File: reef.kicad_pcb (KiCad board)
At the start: 2 copper layers, 85 parts, among them J1 Conn_01x05_Female, J2 Conn_01x02_Male, U1 nice_nano, U2 TRRS, U3 TRRS

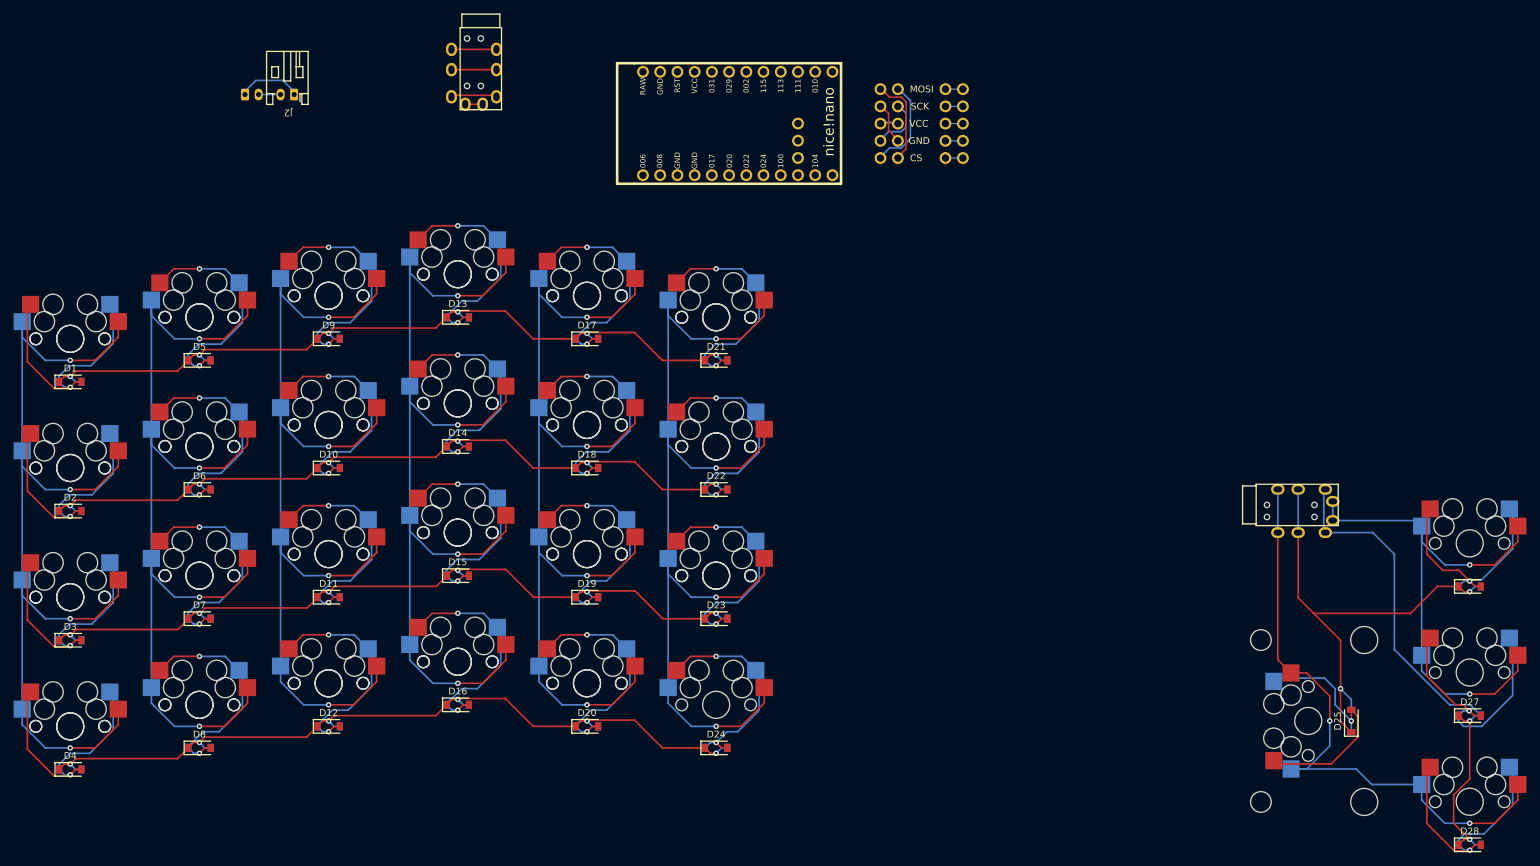
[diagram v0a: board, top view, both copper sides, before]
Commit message: Reversible via Jumper Pads
using solder jumper pads to make component footprints reversible
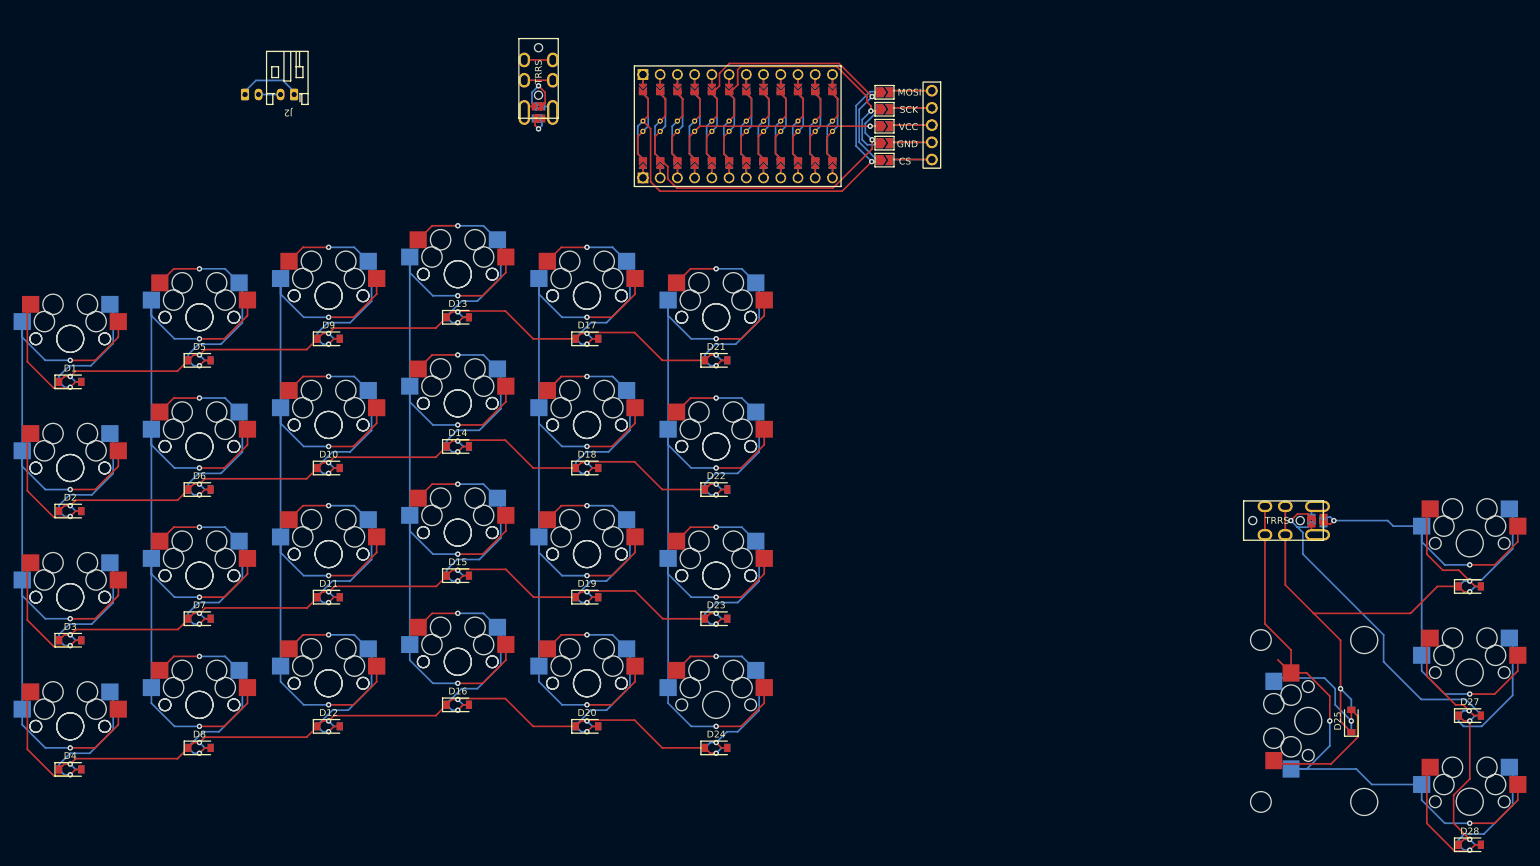
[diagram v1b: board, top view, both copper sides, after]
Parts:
- Display1: moved to F.Cu
- U1: footprint nice-nano-kicad:nice_nano -> keyboard_reversible:ProMicro
- U2, U3: footprint Keebio-Parts:TRRS-PJ-320A -> keyboard_reversible:PJ-320A
- moved U2 8.61 mm to (115.9, 24.6)
- moved Display1 4.57 mm to (188.3, 37.4), turned to -90 degrees
- moved U3 3.16 mm to (219.7, 95.9)
- moved J1 0.91 mm to (166.8, 37.8)
- moved U1 0.40 mm to (145.3, 37.7)
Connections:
- U1 pad 5: sck -> mosi
- U1 pad 6: mosi -> sck
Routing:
- net (no net): track 12.8 -> 63.3 mm
- net cs: track 13.2 -> 59.2 mm, vias 0 -> 1
- net gnd: track 9.38 -> 48.2 mm, vias 0 -> 1
- net sck: track 8.24 -> 36.6 mm, vias 0 -> 1
- net mosi: track 13.8 -> 41.5 mm, vias 0 -> 1
- net vcc: track 2.57 -> 29.0 mm, vias 0 -> 1
- net row_0: track 123.8 -> 121.4 mm
- net col_6: track 6.63 -> 4.20 mm
- net thr_0: track 69.8 -> 68.1 mm
- net thc_7: track 78.5 -> 80.2 mm, vias 2 -> 3
- net thr_1: track 76.3 -> 77.5 mm, vias 2 -> 3
- net thc_6: track 91.3 -> 92.3 mm
- net col_7: track 2.57 -> 3.48 mm, vias 0 -> 1
- net row_1: track 124.0 -> 124.5 mm, vias 6 -> 7

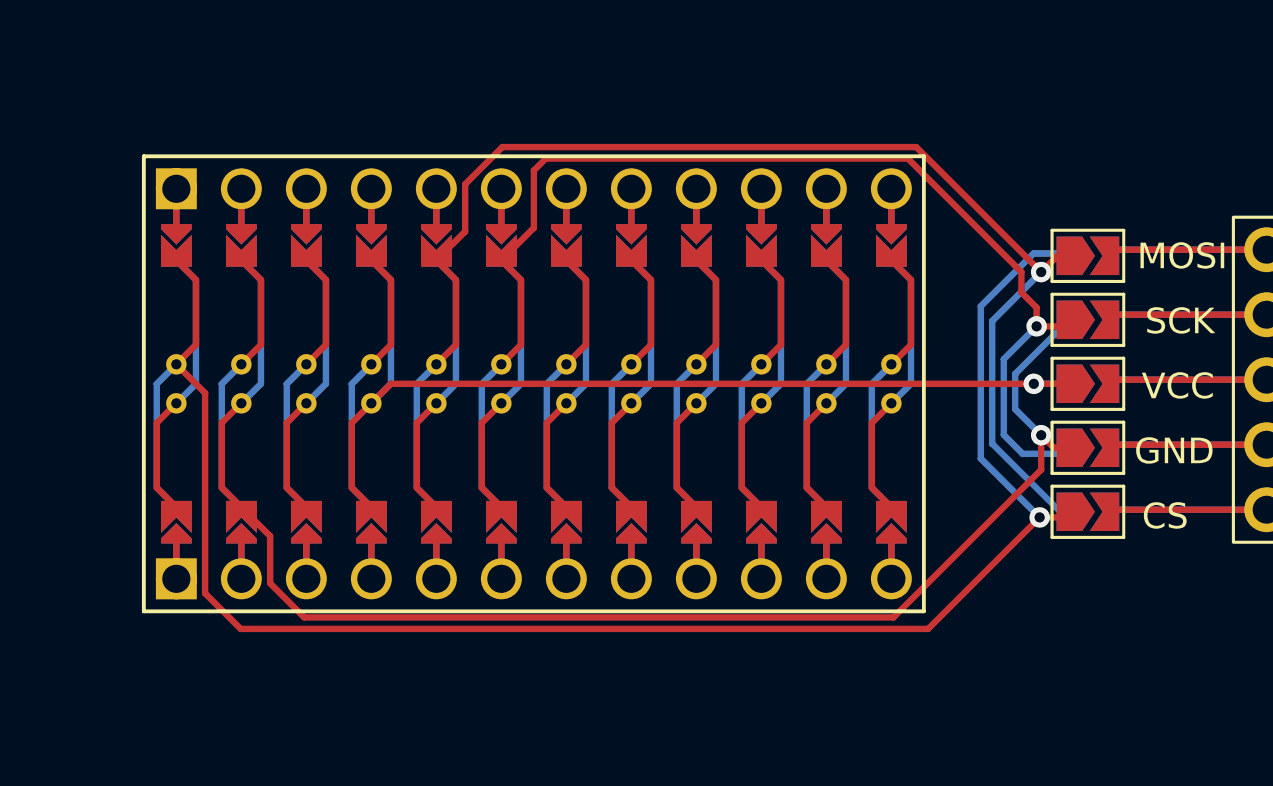
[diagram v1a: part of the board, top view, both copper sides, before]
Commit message: Display Routing
Traces for display should no longer interfere with routing columns and rows to their respective pins in an aesthetically pleasing manner...hopefully
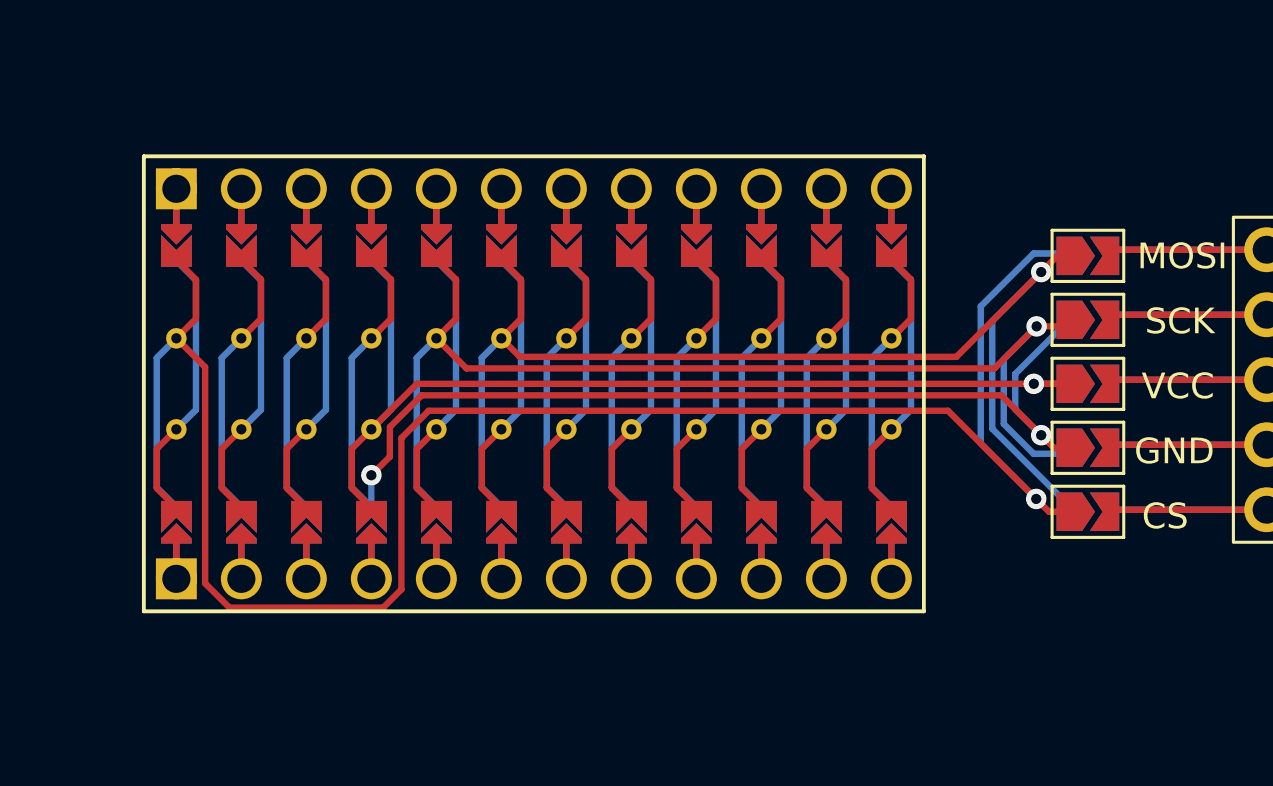
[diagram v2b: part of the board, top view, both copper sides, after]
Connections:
- U1 pad 5: mosi -> sck
- U1 pad 6: sck -> mosi
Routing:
- net gnd: track 48.2 -> 40.4 mm, vias 1 -> 2
- net cs: track 59.2 -> 65.3 mm
- net mosi: track 41.5 -> 35.5 mm
- net sck: track 36.6 -> 33.5 mm

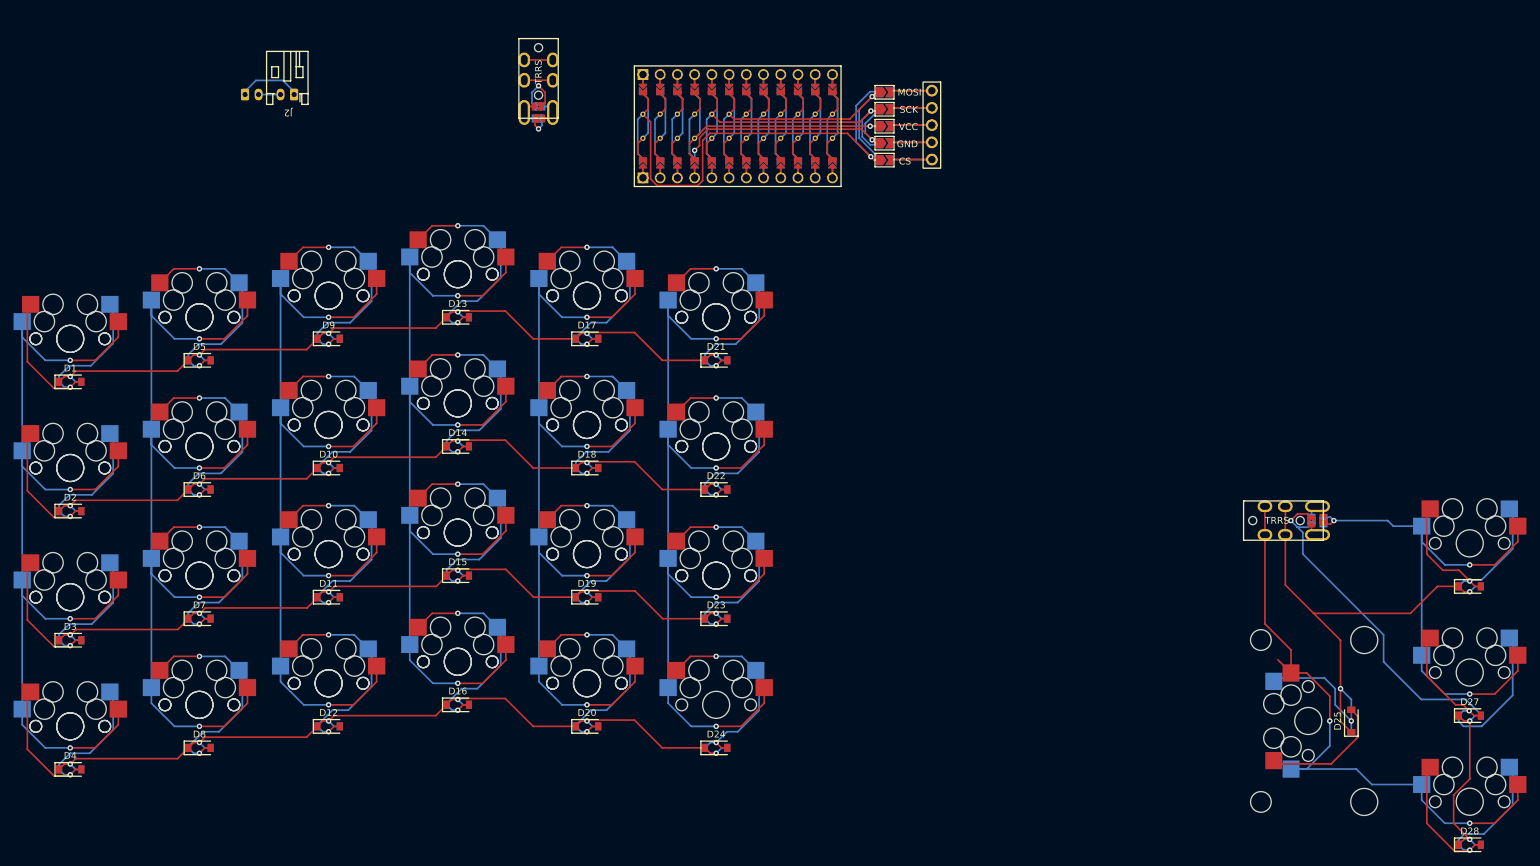
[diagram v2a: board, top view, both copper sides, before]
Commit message: Matrix Reroute
rerouted some matrix traces to connect to vias instead of going through diode pads
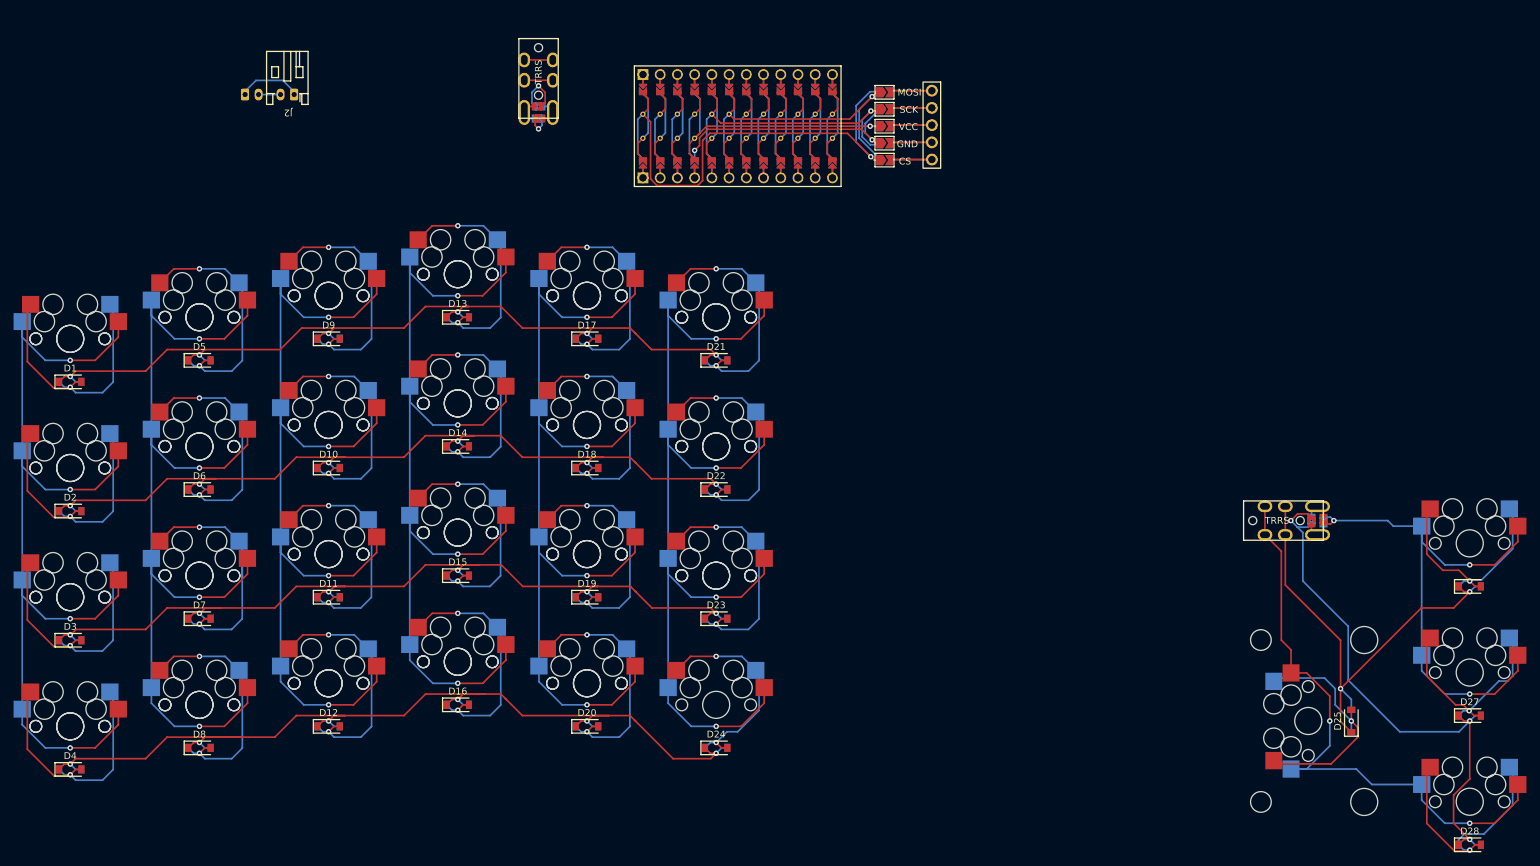
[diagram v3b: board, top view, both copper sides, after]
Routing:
- net row_3: track 117.2 -> 145.1 mm
- net row_2: track 117.2 -> 138.3 mm
- net row_1: track 124.5 -> 144.5 mm
- net row_0: track 121.4 -> 135.9 mm
- net Net-(D7-Pad2): track 34.0 -> 41.4 mm
- net Net-(D27-Pad2): track 37.7 -> 32.4 mm
- net thr_1: track 77.5 -> 82.0 mm
- net Net-(D17-Pad2): track 33.6 -> 36.5 mm
- net Net-(D13-Pad2): track 33.6 -> 36.5 mm
- net thc_6: track 92.3 -> 89.6 mm
- net Net-(D19-Pad2): track 33.6 -> 36.3 mm
- net Net-(D20-Pad2): track 33.6 -> 36.3 mm
- net Net-(D12-Pad2): track 33.6 -> 36.3 mm
- net Net-(D8-Pad2): track 33.6 -> 36.3 mm
- net Net-(D16-Pad2): track 33.6 -> 36.3 mm
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
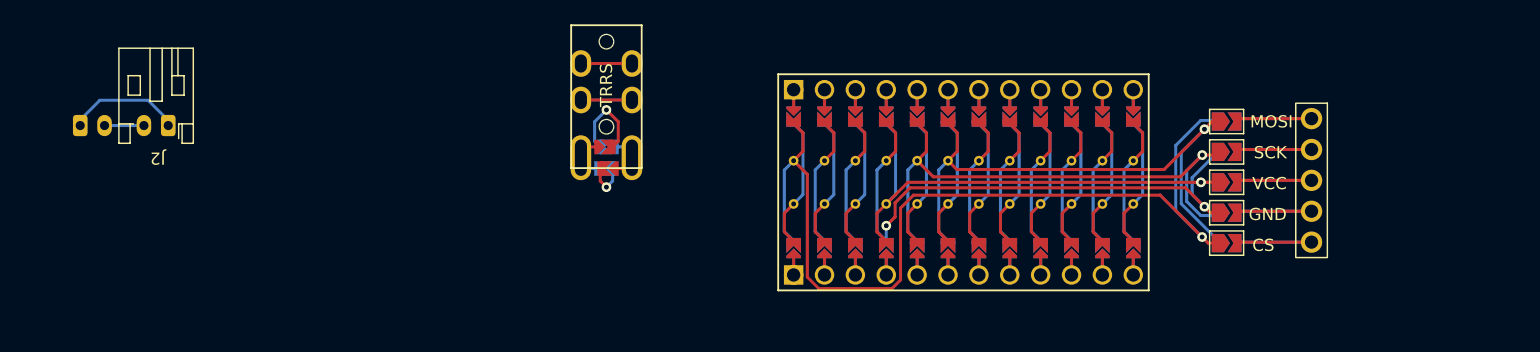
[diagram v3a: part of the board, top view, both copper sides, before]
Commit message: Routed Battery Connector
routed traces for battery connector
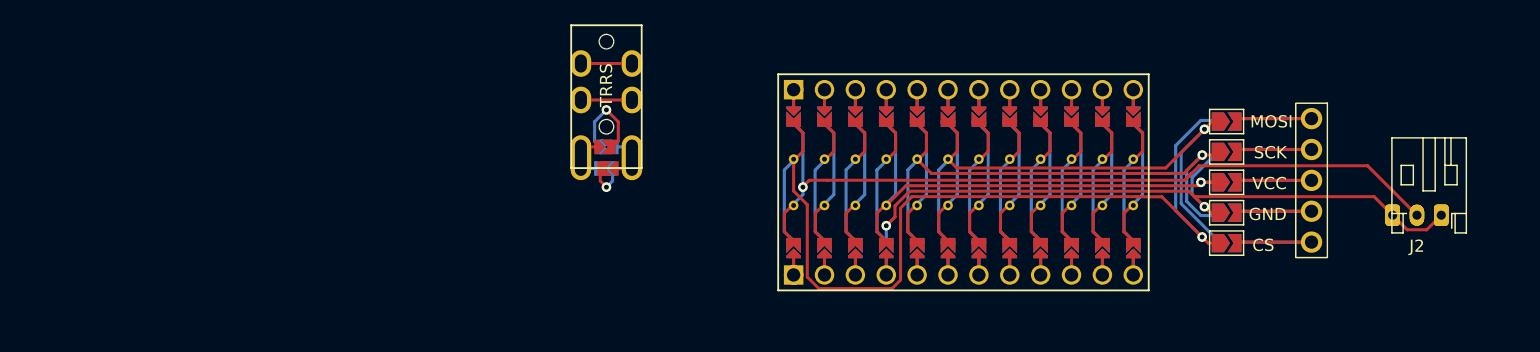
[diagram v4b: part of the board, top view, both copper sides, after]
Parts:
- J2: moved to F.Cu
- moved J2 109.3 mm to (182.6, 37.4), turned to 180 degrees
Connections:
- J2 pad 1: bat+ -> gnd
- J2 pad 2: gnd -> bat+
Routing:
- net bat+: track 9.48 -> 53.5 mm, vias 0 -> 1
- net gnd: track 40.4 -> 58.7 mm
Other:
- board text removed: "J2"

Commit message: Reset and Power switches in progress
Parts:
- moved U2 109.7 mm to (225.4, 30.2)
- moved J2 5.78 mm to (188.3, 37.4)
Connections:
- U1 pad 10: col_6 -> row_1
- U1 pad 11: col_0 -> row_2
- U1 pad 12: col_1 -> row_3
- U1 pad 13: col_5 -> col_7
- U1 pad 14: col_4 -> col_6
- U1 pad 15: col_3 -> col_5
- U1 pad 16: col_2 -> col_4
- U1 pad 17: row_3 -> col_3
- U1 pad 18: row_2 -> col_2
- U1 pad 19: row_1 -> col_1
- U1 pad 20: row_0 -> col_0
- U1 pad 9: col_7 -> row_0
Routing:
- net row_3: track 145.1 -> 158.9 mm
- net row_2: track 138.3 -> 151.0 mm
- net row_1: track 144.5 -> 156.1 mm
- net row_0: track 135.9 -> 145.1 mm
- net bat+: track 53.5 -> 47.8 mm
- net gnd: track 58.7 -> 57.1 mm
- net sck: track 33.4 -> 34.3 mm
- net cs: track 65.3 -> 65.9 mm
- net vcc: track 29.7 -> 29.1 mm

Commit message: Power and Reset footprints
added footprints for power and reset switches to PCB
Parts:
- added SW0: B3U-1000P[], footprints_buttonSwitch:SW_B3U-1000P_OMR, F.Cu at (206.4, 57.1)
- added SW1: PCM12SMTR, PCM12SMTR:SW_PCM12SMTR, F.Cu at (181.8, 58.4)
- J1: value Conn_01x05_Female -> nice!view sockets
- J2: value Conn_01x02_Male -> battery connector
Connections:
- J2 pad 2: bat+ -> bat_sw+
- U1 pad 22: unconnected-(U1-Pad22) -> rst
